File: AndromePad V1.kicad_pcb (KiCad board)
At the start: 2 copper layers, 48 parts, among them SW1 keyswitch, SW10 keyswitch, SW11 keyswitch, SW2 keyswitch, SW21 RotaryEncoder_Switch, SW22 RotaryEncoder_Switch, SW3 keyswitch, SW5 keyswitch, SW6 keyswitch, SW7 keyswitch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

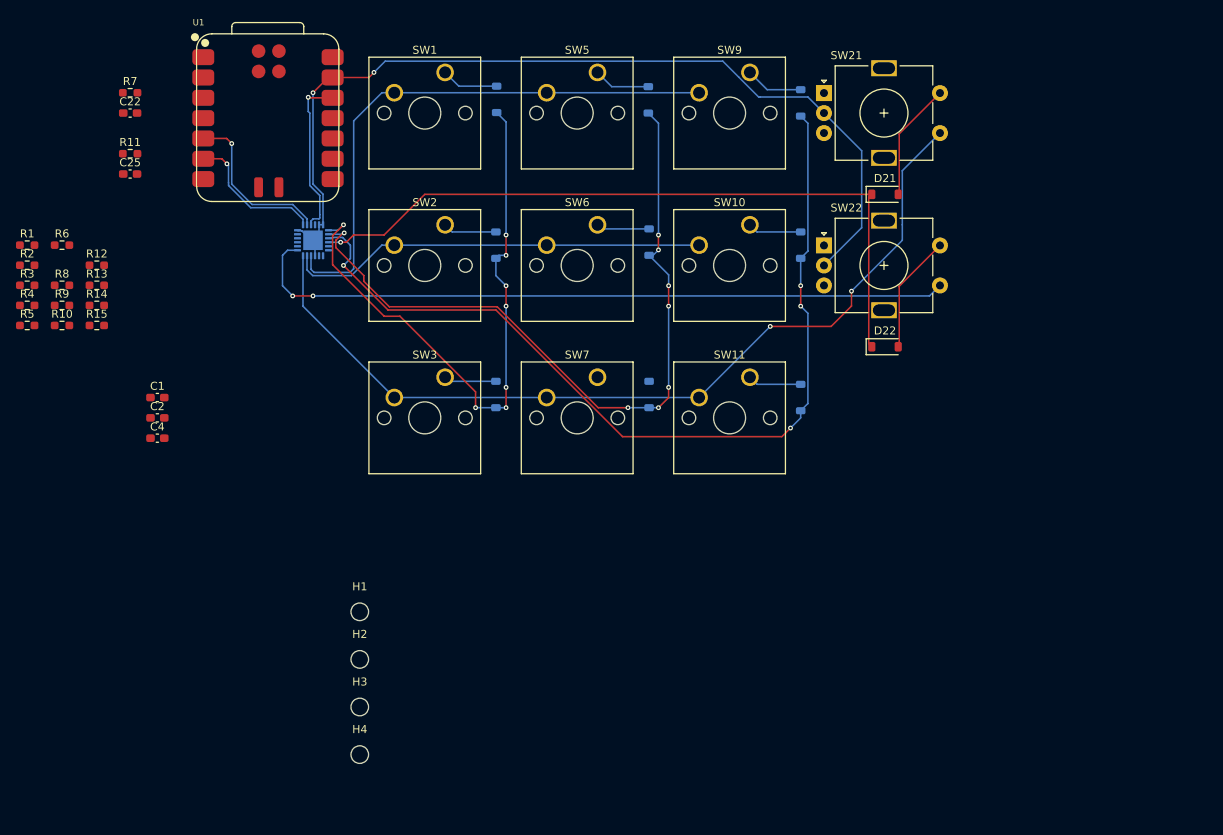
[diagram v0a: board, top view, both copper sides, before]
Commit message: finished routing in the pcb editor
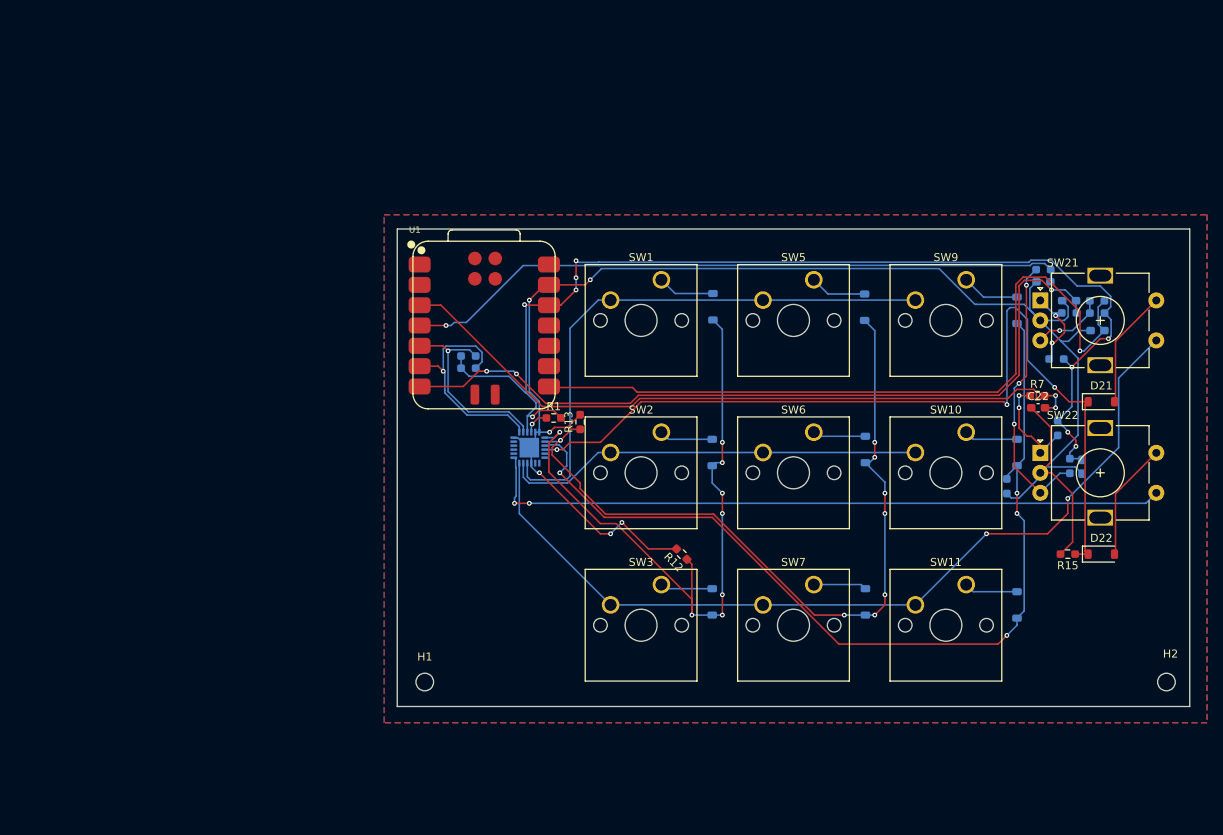
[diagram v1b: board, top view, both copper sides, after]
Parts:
- removed H3, H4: MountingHole, MountingHole:MountingHole_2.2mm_M2
- C1, C2, C25, C4, R10, R11, R14, R2, R3, R4, R5, R6, R8, R9: moved to B.Cu
- moved R5 133.8 mm to (185.7, 79.6), turned to 180 degrees
- moved R4 130.2 mm to (182.1, 79.6)
- moved R6 129.6 mm to (185.6, 78.1), turned to 180 degrees
- moved R10 127.2 mm to (182.2, 98.7), turned to -90 degrees
- moved R9 125.4 mm to (180.7, 94.0), turned to -90 degrees
- moved R15 124.7 mm to (182.0, 109.7), turned to 180 degrees
- moved R8 124.6 mm to (180.6, 85.4), turned to 180 degrees
- moved R7 119.6 mm to (178.2, 89.9)
- moved C22 119.3 mm to (178.3, 91.5)
- moved C2 118.0 mm to (185.7, 81.8), turned to 180 degrees
- moved R14 116.0 mm to (174.4, 101.3), turned to -90 degrees
- moved C1 115.9 mm to (183.8, 98.8), turned to -90 degrees
- moved C4 115.3 mm to (182.1, 78.1)
- moved R11 115.1 mm to (178.9, 74.2), turned to 180 degrees
- moved C25 115.0 mm to (178.9, 75.7), turned to 180 degrees
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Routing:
- net +3V3: track 20.5 -> 141.3 mm, vias 1 -> 9
- net /ENC_A: track 0.00 -> 100.0 mm, vias 0 -> 3
- net /ENC_B: track 0.00 -> 94.3 mm, vias 0 -> 1
- net /ENC2_A: track 0.00 -> 89.6 mm, vias 0 -> 2
- net /ENC2_B: track 0.00 -> 84.0 mm, vias 0 -> 1
- net GND: track 115.2 -> 196.0 mm, vias 2 -> 6
- net Net-(R10-Pad2): track 0.00 -> 35.1 mm, vias 0 -> 3
- net /ROW4: track 89.8 -> 111.3 mm, vias 1 -> 3
- net Net-(R7-Pad1): track 0.00 -> 13.0 mm, vias 0 -> 2
- net Net-(R4-Pad1): track 0.00 -> 11.1 mm, vias 0 -> 2
- net /SCL: track 17.7 -> 28.2 mm
- net Net-(R5-Pad2): track 0.00 -> 9.15 mm, vias 0 -> 1
- net /ROW1: track 76.9 -> 84.1 mm
- net Net-(D7-A): track 0.00 -> 6.66 mm
- net /SDA: track 20.8 -> 24.7 mm
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- added copper zone on B.Cu, net (none)
- added copper zone on F.Cu, net (none)
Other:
- board outline added: 99.1 x 59.7 mm

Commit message: feat: updated layout in pcb editor (much cleaner layout and better routing than before)
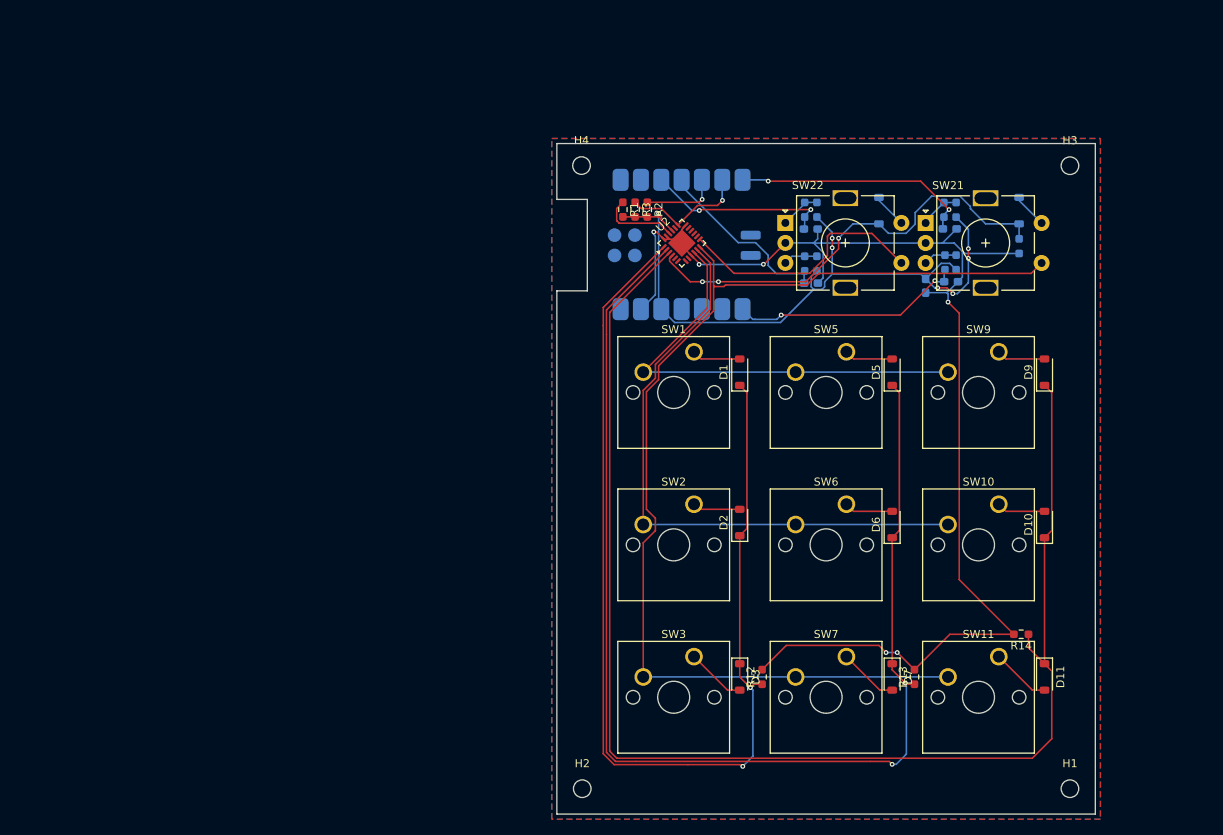
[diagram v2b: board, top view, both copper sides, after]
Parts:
- added H3: MountingHole, MountingHole:MountingHole_2.2mm_M2, F.Cu at (182.2, 61.2)
- added H4: MountingHole, MountingHole:MountingHole_2.2mm_M2, F.Cu at (121.2, 61.2)
- C22, D21, D22, R15, R7, U1: moved to B.Cu
- D1, D10, D11, D2, D3, D5, D6, D7, D9, R14, R2, R3, U2: moved to F.Cu
- moved H1 81.7 mm to (182.2, 139.1)
- moved H2 74.2 mm to (121.3, 139.1)
- moved R13 52.6 mm to (162.8, 125.1)
- moved D22 51.2 mm to (158.4, 66.8), turned to 90 degrees
- moved SW22 42.9 mm to (146.7, 68.3)
- moved R9 40.6 mm to (150.6, 66.7), turned to 90 degrees
- moved R10 40.5 mm to (150.6, 73.4), turned to 90 degrees
- moved R15 39.0 mm to (175.9, 71.2), turned to -90 degrees
- moved R7 37.2 mm to (149.1, 66.7), turned to -90 degrees
- moved C22 36.2 mm to (149.8, 69.1), turned to 180 degrees
- moved U2 31.9 mm to (133.7, 70.9), turned to 45 degrees
- moved C1 29.9 mm to (164.2, 76.2)
- moved R11 29.9 mm to (149.1, 73.4), turned to 90 degrees
- moved C25 29.1 mm to (149.9, 75.9), turned to 0 degrees
- moved R2 28.9 mm to (129.4, 66.7), turned to -90 degrees
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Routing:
- net /ENC_A: track 100.0 -> 30.1 mm, vias 3 -> 2
- net /ENC2_A: track 89.6 -> 23.1 mm
- net /ENC_B: track 94.3 -> 29.3 mm, vias 1 -> 2
- net /ENC2_B: track 84.0 -> 23.1 mm, vias 1 -> 0
- net /ROW3: track 114.4 -> 171.9 mm, vias 4 -> 0
- net /ROW2: track 96.1 -> 153.4 mm, vias 8 -> 2
- net /ROW4: track 111.3 -> 56.1 mm
- net /COL4: track 86.7 -> 32.0 mm, vias 2 -> 0
- net +3V3: track 141.3 -> 87.9 mm, vias 9 -> 7
- net /ROW1: track 84.1 -> 135.8 mm, vias 8 -> 2
- net GND: track 196.0 -> 163.7 mm
- net Net-(R10-Pad2): track 35.1 -> 4.28 mm, vias 3 -> 0
- net /COL3: track 110.5 -> 139.4 mm, vias 2 -> 0
- net /COL2: track 52.7 -> 76.6 mm
- net /SDA: track 24.7 -> 9.47 mm
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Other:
- board size 99.1 x 59.7 mm -> 67.3 x 83.8 mm
